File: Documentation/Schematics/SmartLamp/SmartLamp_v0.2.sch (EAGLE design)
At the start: 26 parts, among them IC1 DS3231/SO, J1 POWER_JACKPTH_BREAD, Q1 IRF1404, Q2 IRF1404, Q3 IRF1404, U1 HM-10

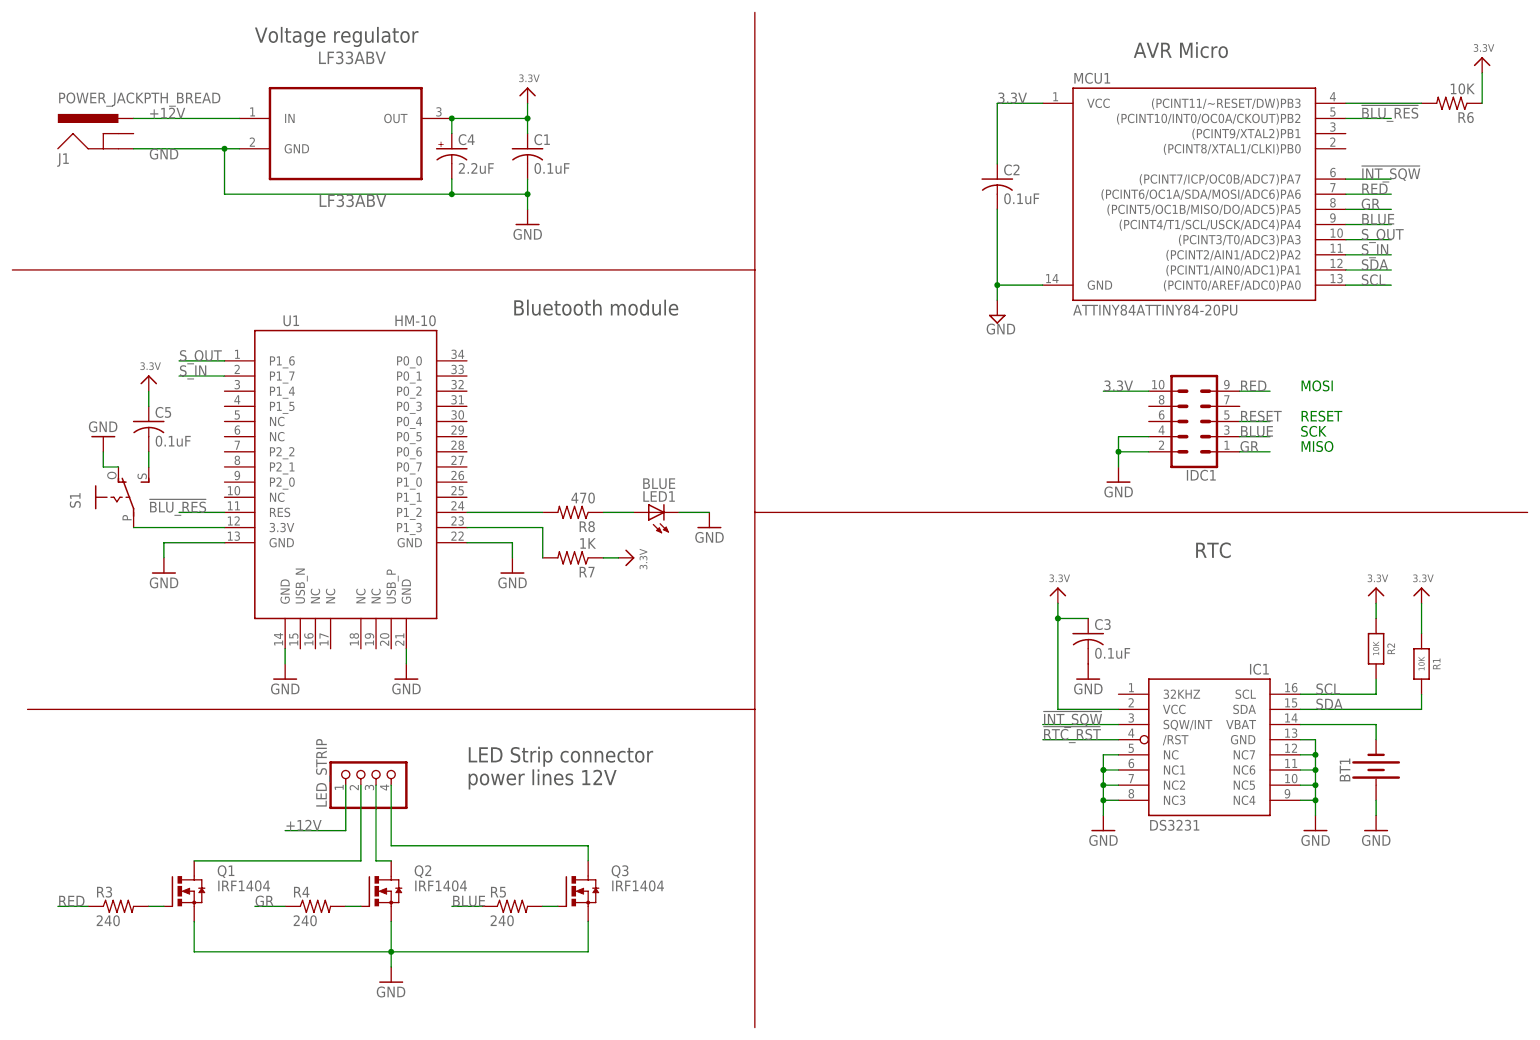
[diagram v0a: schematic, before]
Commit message: Modified switch and RGB connection
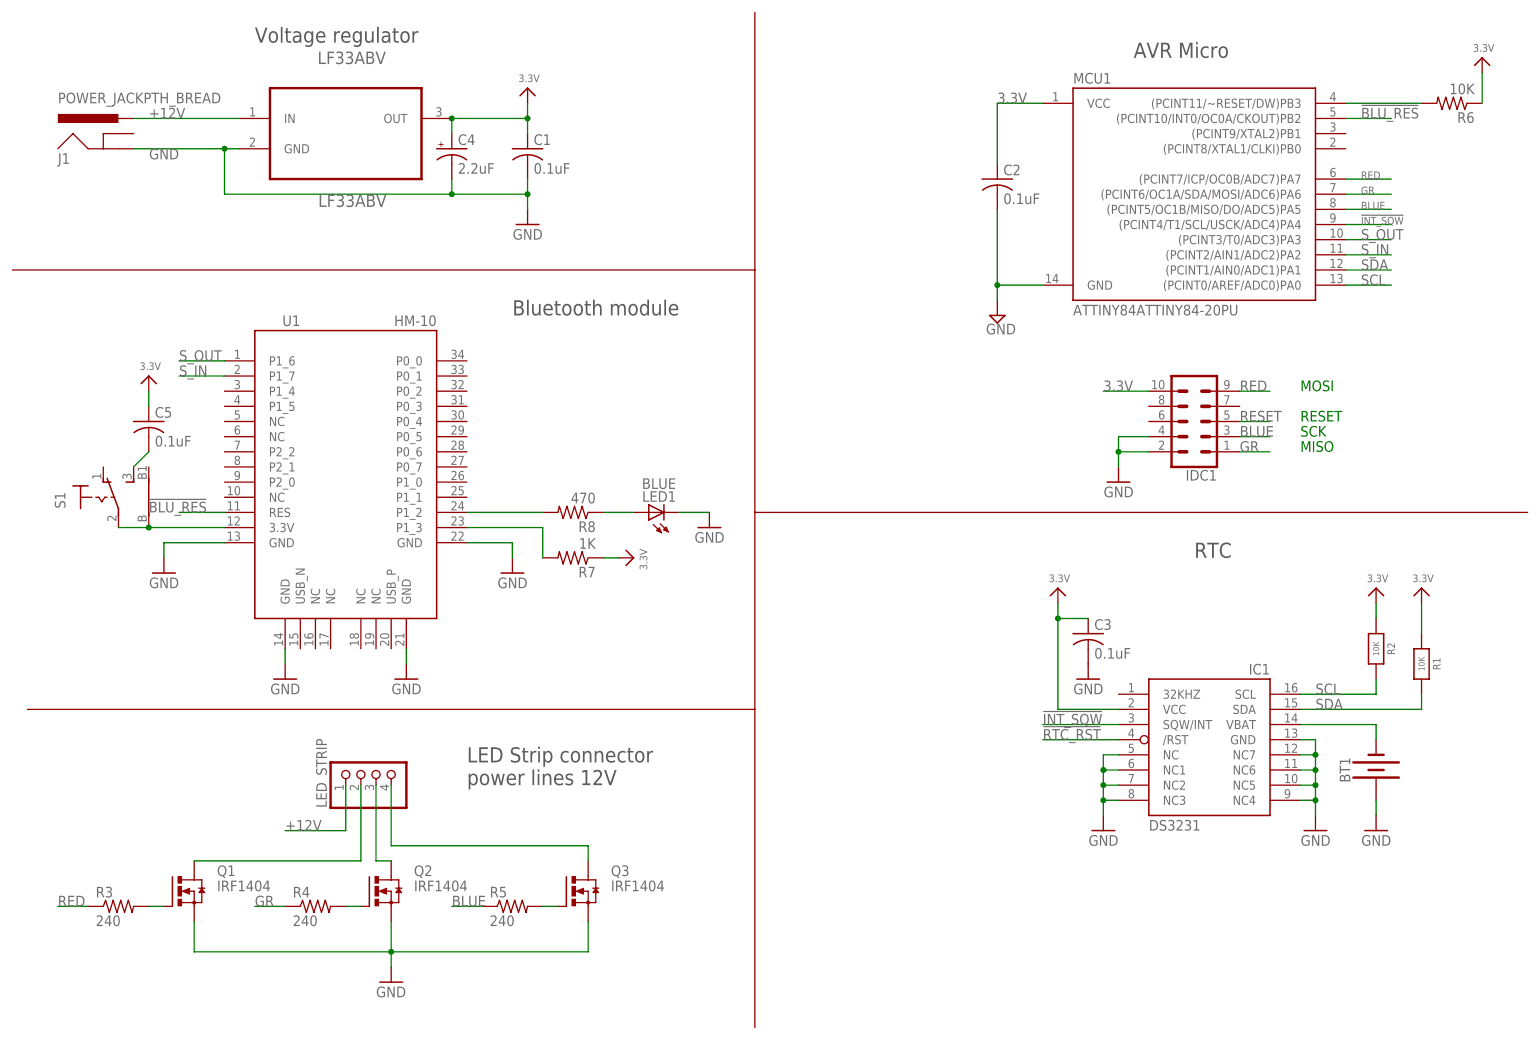
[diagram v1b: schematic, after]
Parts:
- S1: device adafruit:EG1218S -> switch:9070-1W
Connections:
- net !INT_SQW: now also MCU1.(PCINT4/T1/SCL/USCK/ADC4)PA4; no longer MCU1.(PCINT7/ICP/OC0B/ADC7)PA7
- net BLUE: now also MCU1.(PCINT5/OC1B/MISO/DO/ADC5)PA5; no longer MCU1.(PCINT4/T1/SCL/USCK/ADC4)PA4
- net GND: no longer S1.O
- net GR: now also MCU1.(PCINT6/OC1A/SDA/MOSI/ADC6)PA6; no longer MCU1.(PCINT5/OC1B/MISO/DO/ADC5)PA5
- net N$1: now also S1.B
- net RED: now also MCU1.(PCINT7/ICP/OC0B/ADC7)PA7; no longer MCU1.(PCINT6/OC1A/SDA/MOSI/ADC6)PA6
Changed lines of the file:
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@@
 <part name="U$8" library="microbuilder" deviceset="3.3V" device=""/>
 <part name="C5" library="adafruit" deviceset="C-US" device="025-024X044" value="0.1uF"/>
-<part name="S1" library="adafruit" deviceset="EG1218" device="S"/>
-<part name="GND6" library="supply1" deviceset="GND" device=""/>
+<part name="S1" library="switch" deviceset="9070-1W" device=""/>
 <part name="Q1" library="transistor-power" deviceset="IRFI540NPBF" device="" value="IRF1404"/>
 <part name="Q2" library="transistor-power" deviceset="IRFI540NPBF" device="" value="IRF1404"/>
@@
 <instance part="U$8" gate="G$1" x="106.68" y="83.82" rot="R270"/>
 <instance part="C5" gate="G$1" x="25.4" y="106.68"/>
-<instance part="S1" gate="1" x="20.32" y="93.98"/>
-<instance part="GND6" gate="1" x="17.78" y="104.14" rot="MR180"/>
+<instance part="S1" gate="2" x="17.78" y="93.98"/>
 <instance part="Q1" gate="G$1" x="30.48" y="27.94"/>
 <instance part="Q2" gate="G$1" x="63.5" y="27.94"/>
@@
 </segment>
 <segment>
-<pinref part="S1" gate="1" pin="O"/>
-<pinref part="GND6" gate="1" pin="GND"/>
-<wire x1="20.32" y1="99.06" x2="17.78" y2="99.06" width="0.1524" layer="91"/>
-<wire x1="17.78" y1="99.06" x2="17.78" y2="101.6" width="0.1524" layer="91"/>
-</segment>
-<segment>
 <pinref part="Q1" gate="G$1" pin="S"/>
 <wire x1="33.02" y1="22.86" x2="33.02" y2="17.78" width="0.1524" layer="91"/>
@@
 </segment>
 <segment>
-<pinref part="MCU1" gate="G$1" pin="(PCINT7/ICP/OC0B/ADC7)PA7"/>
-<wire x1="226.06" y1="147.32" x2="233.68" y2="147.32" width="0.1524" layer="91"/>
-<label x="228.6" y="147.32" size="1.778" layer="95"/>
+<pinref part="MCU1" gate="G$1" pin="(PCINT4/T1/SCL/USCK/ADC4)PA4"/>
+<wire x1="226.06" y1="139.7" x2="233.68" y2="139.7" width="0.1524" layer="91"/>
+<label x="228.6" y="139.7" size="1.27" layer="95" font="vector"/>
 </segment>
 </net>
@@
 <net name="N$1" class="0">
 <segment>
-<pinref part="S1" gate="1" pin="P"/>
+<pinref part="S1" gate="2" pin="P"/>
 <pinref part="U1" gate="G$1" pin="3.3V"/>
-<wire x1="22.86" y1="88.9" x2="38.1" y2="88.9" width="0.1524" layer="91"/>
+<wire x1="20.32" y1="88.9" x2="25.4" y2="88.9" width="0.1524" layer="91"/>
+<pinref part="S1" gate="2" pin="B"/>
+<wire x1="25.4" y1="88.9" x2="38.1" y2="88.9" width="0.1524" layer="91"/>
+<junction x="25.4" y="88.9"/>
 </segment>
 </net>
@@
 <segment>
 <pinref part="C5" gate="G$1" pin="2"/>
-<pinref part="S1" gate="1" pin="S"/>
-<wire x1="25.4" y1="101.6" x2="25.4" y2="99.06" width="0.1524" layer="91"/>
+<pinref part="S1" gate="2" pin="S"/>
+<wire x1="25.4" y1="101.6" x2="22.86" y2="99.06" width="0.1524" layer="91"/>
 </segment>
 </net>
@@
 </segment>
 <segment>
-<pinref part="MCU1" gate="G$1" pin="(PCINT6/OC1A/SDA/MOSI/ADC6)PA6"/>
-<wire x1="226.06" y1="144.78" x2="233.68" y2="144.78" width="0.1524" layer="91"/>
-<label x="228.6" y="144.78" size="1.778" layer="95"/>
-</segment>
-<segment>
 <pinref part="IDC1" gate="G$1" pin="9"/>
 <wire x1="208.28" y1="111.76" x2="213.36" y2="111.76" width="0.1524" layer="91"/>
 <label x="208.28" y="111.76" size="1.778" layer="95"/>
 </segment>
+<segment>
+<pinref part="MCU1" gate="G$1" pin="(PCINT7/ICP/OC0B/ADC7)PA7"/>
+<wire x1="226.06" y1="147.32" x2="233.68" y2="147.32" width="0.1524" layer="91"/>
+<label x="228.6" y="147.32" size="1.27" layer="95" font="vector"/>
+</segment>
 </net>
 <net name="GR" class="0">
@@
 </segment>
 <segment>
-<pinref part="MCU1" gate="G$1" pin="(PCINT5/OC1B/MISO/DO/ADC5)PA5"/>
-<wire x1="226.06" y1="142.24" x2="233.68" y2="142.24" width="0.1524" layer="91"/>
-<label x="228.6" y="142.24" size="1.778" layer="95"/>
-</segment>
-<segment>
 <pinref part="IDC1" gate="G$1" pin="1"/>
 <wire x1="208.28" y1="101.6" x2="213.36" y2="101.6" width="0.1524" layer="91"/>
 <label x="208.28" y="101.6" size="1.778" layer="95"/>
 </segment>
+<segment>
+<pinref part="MCU1" gate="G$1" pin="(PCINT6/OC1A/SDA/MOSI/ADC6)PA6"/>
+<wire x1="226.06" y1="144.78" x2="233.68" y2="144.78" width="0.1524" layer="91"/>
+<label x="228.6" y="144.78" size="1.27" layer="95" font="vector"/>
+</segment>
 </net>
 <net name="BLUE" class="0">
@@
 </segment>
 <segment>
-<pinref part="MCU1" gate="G$1" pin="(PCINT4/T1/SCL/USCK/ADC4)PA4"/>
-<wire x1="226.06" y1="139.7" x2="233.68" y2="139.7" width="0.1524" layer="91"/>
-<label x="228.6" y="139.7" size="1.778" layer="95"/>
-</segment>
-<segment>
 <pinref part="IDC1" gate="G$1" pin="3"/>
 <wire x1="208.28" y1="104.14" x2="213.36" y2="104.14" width="0.1524" layer="91"/>
 <label x="208.28" y="104.14" size="1.778" layer="95"/>
 </segment>
-</net>
+<segment>
+<pinref part="MCU1" gate="G$1" pin="(PCINT5/OC1B/MISO/DO/ADC5)PA5"/>
+<wire x1="226.06" y1="142.24" x2="233.68" y2="142.24" width="0.1524" layer="91"/>
+<label x="228.6" y="142.24" size="1.27" layer="95" font="vector"/>
+</segment>
+</net>

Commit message: Fixed IDC connector and replaced switch
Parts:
- removed S1: (no value), switch:9070-1W
- added S2: 219-02, switch-dil:219-02
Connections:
- new net S_OUT_DEBUG: IDC1.6, MCU1.(PCINT9/XTAL2)PB1
- net !INT_SQW: now also IDC1.7
- net 3.3V: now also IDC1.2, S2.1; no longer C5.1, IDC1.10
- net BLUE: now also IDC1.9; no longer IDC1.3
- net GND: now also IDC1.10, IDC1.8; no longer IDC1.2, IDC1.4
- net N$1: now also C5.2; no longer S1.B, S1.P
- net N$2: now also C5.1, S2.4; no longer C5.2, S1.S
- net RED: no longer IDC1.9
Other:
- moved on the sheet: C5, IDC1
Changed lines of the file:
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@@
 <part name="U$8" library="microbuilder" deviceset="3.3V" device=""/>
 <part name="C5" library="adafruit" deviceset="C-US" device="025-024X044" value="0.1uF"/>
-<part name="S1" library="switch" deviceset="9070-1W" device=""/>
 <part name="Q1" library="transistor-power" deviceset="IRFI540NPBF" device="" value="IRF1404"/>
 <part name="Q2" library="transistor-power" deviceset="IRFI540NPBF" device="" value="IRF1404"/>
@@
 <part name="BT1" library="SparkFun-Batteries" deviceset="BATTERY" device="-20MM_SMD_4LEGS"/>
 <part name="GND13" library="supply1" deviceset="GND" device=""/>
+<part name="S2" library="switch-dil" deviceset="219-02*" device=""/>
 </parts>
 <sheets>
 <sheet>
 <plain>
-<text x="218.44" y="111.76" size="1.778" layer="91">MOSI</text>
-<text x="218.44" y="104.14" size="1.778" layer="91">SCK</text>
-<text x="218.44" y="101.6" size="1.778" layer="91">MISO</text>
-<text x="218.44" y="106.68" size="1.778" layer="91">RESET</text>
+<text x="172.72" y="111.76" size="1.778" layer="91">MOSI</text>
+<text x="172.72" y="104.14" size="1.778" layer="91">SCK</text>
+<text x="172.72" y="101.6" size="1.778" layer="91">MISO</text>
+<text x="172.72" y="106.68" size="1.778" layer="91">RESET</text>
 <wire x1="2.54" y1="132.08" x2="127" y2="132.08" width="0.1524" layer="94"/>
 <wire x1="127" y1="132.08" x2="127" y2="175.26" width="0.1524" layer="94"/>
@@
 <instance part="R8" gate="G$1" x="96.52" y="91.44" rot="R180"/>
 <instance part="LED1" gate="G$1" x="109.22" y="91.44" rot="R90"/>
-<instance part="U$7" gate="G$1" x="25.4" y="114.3"/>
+<instance part="U$7" gate="G$1" x="15.24" y="121.92"/>
 <instance part="GND7" gate="1" x="27.94" y="81.28" rot="MR0"/>
 <instance part="GND8" gate="1" x="48.26" y="63.5" rot="MR0"/>
@@
 <instance part="GND12" gate="1" x="119.38" y="88.9" rot="MR0"/>
 <instance part="U$8" gate="G$1" x="106.68" y="83.82" rot="R270"/>
-<instance part="C5" gate="G$1" x="25.4" y="106.68"/>
-<instance part="S1" gate="2" x="17.78" y="93.98"/>
+<instance part="C5" gate="G$1" x="15.24" y="96.52"/>
 <instance part="Q1" gate="G$1" x="30.48" y="27.94"/>
 <instance part="Q2" gate="G$1" x="63.5" y="27.94"/>
@@
 <instance part="R4" gate="G$1" x="53.34" y="25.4"/>
 <instance part="R5" gate="G$1" x="86.36" y="25.4"/>
-<instance part="IDC1" gate="G$1" x="200.66" y="106.68" rot="R180"/>
-<instance part="GND14" gate="1" x="187.96" y="96.52" rot="MR0"/>
+<instance part="IDC1" gate="G$1" x="200.66" y="106.68"/>
+<instance part="GND14" gate="1" x="215.9" y="96.52" rot="MR0"/>
 <instance part="J1" gate="G$1" x="20.32" y="149.86"/>
 <instance part="C1" gate="G$1" x="88.9" y="152.4"/>
@@
 <instance part="BT1" gate="G$1" x="231.14" y="48.26" rot="R90"/>
 <instance part="GND13" gate="1" x="231.14" y="38.1" rot="MR0"/>
+<instance part="S2" gate="G$1" x="15.24" y="109.22" rot="R180"/>
 </instances>
 <busses>
@@
 </segment>
 <segment>
-<pinref part="IDC1" gate="G$1" pin="4"/>
-<wire x1="193.04" y1="104.14" x2="187.96" y2="104.14" width="0.1524" layer="91"/>
-<pinref part="IDC1" gate="G$1" pin="2"/>
-<wire x1="193.04" y1="101.6" x2="187.96" y2="101.6" width="0.1524" layer="91"/>
-<wire x1="187.96" y1="101.6" x2="187.96" y2="104.14" width="0.1524" layer="91"/>
-<wire x1="187.96" y1="101.6" x2="187.96" y2="99.06" width="0.1524" layer="91"/>
-<junction x="187.96" y="101.6"/>
-<pinref part="GND14" gate="1" pin="GND"/>
-</segment>
-<segment>
 <pinref part="GND4" gate="1" pin="GND"/>
 <pinref part="C3" gate="G$1" pin="2"/>
@@
 <pinref part="GND13" gate="1" pin="GND"/>
 <wire x1="231.14" y1="43.18" x2="231.14" y2="40.64" width="0.1524" layer="91"/>
+</segment>
+<segment>
+<pinref part="IDC1" gate="G$1" pin="8"/>
+<wire x1="208.28" y1="104.14" x2="215.9" y2="104.14" width="0.1524" layer="91"/>
+<pinref part="IDC1" gate="G$1" pin="10"/>
+<wire x1="208.28" y1="101.6" x2="215.9" y2="101.6" width="0.1524" layer="91"/>
+<wire x1="215.9" y1="101.6" x2="215.9" y2="104.14" width="0.1524" layer="91"/>
+<pinref part="GND14" gate="1" pin="GND"/>
+<wire x1="215.9" y1="101.6" x2="215.9" y2="99.06" width="0.1524" layer="91"/>
+<junction x="215.9" y="101.6"/>
 </segment>
 </net>
@@
 </segment>
 <segment>
+<pinref part="IDC1" gate="G$1" pin="2"/>
+<wire x1="208.28" y1="111.76" x2="215.9" y2="111.76" width="0.1524" layer="91"/>
+<label x="210.82" y="111.76" size="1.778" layer="95" font="vector"/>
+</segment>
+<segment>
 <pinref part="U$7" gate="G$1" pin="3.3V"/>
-<pinref part="C5" gate="G$1" pin="1"/>
-<wire x1="25.4" y1="111.76" x2="25.4" y2="109.22" width="0.1524" layer="91"/>
-</segment>
-<segment>
-<pinref part="IDC1" gate="G$1" pin="10"/>
-<wire x1="193.04" y1="111.76" x2="185.42" y2="111.76" width="0.1524" layer="91"/>
-<label x="185.42" y="111.76" size="1.778" layer="95"/>
+<pinref part="S2" gate="G$1" pin="1"/>
+<wire x1="15.24" y1="119.38" x2="15.24" y2="116.84" width="0.1524" layer="91"/>
 </segment>
 </net>
@@
 <pinref part="MCU1" gate="G$1" pin="(PCINT4/T1/SCL/USCK/ADC4)PA4"/>
 <wire x1="226.06" y1="139.7" x2="233.68" y2="139.7" width="0.1524" layer="91"/>
-<label x="228.6" y="139.7" size="1.27" layer="95" font="vector"/>
+<label x="228.6" y="139.7" size="1.778" layer="95" font="vector"/>
+</segment>
+<segment>
+<pinref part="IDC1" gate="G$1" pin="7"/>
+<wire x1="193.04" y1="104.14" x2="182.88" y2="104.14" width="0.1524" layer="91"/>
+<label x="182.88" y="104.14" size="1.778" layer="95" font="vector"/>
 </segment>
 </net>
@@
 <pinref part="R6" gate="G$1" pin="2"/>
 <wire x1="226.06" y1="160.02" x2="238.76" y2="160.02" width="0.1524" layer="91"/>
+<label x="228.6" y="160.02" size="1.778" layer="95"/>
 </segment>
 <segment>
 <pinref part="IDC1" gate="G$1" pin="5"/>
-<wire x1="208.28" y1="106.68" x2="213.36" y2="106.68" width="0.1524" layer="91"/>
-<label x="208.28" y="106.68" size="1.778" layer="95"/>
+<wire x1="193.04" y1="106.68" x2="182.88" y2="106.68" width="0.1524" layer="91"/>
+<label x="182.88" y="106.68" size="1.778" layer="95" font="vector"/>
 </segment>
 </net>
@@
 <pinref part="R7" gate="G$1" pin="2"/>
 <wire x1="91.44" y1="88.9" x2="91.44" y2="83.82" width="0.1524" layer="91"/>
-</segment>
-</net>
-<net name="N$1" class="0">
-<segment>
-<pinref part="S1" gate="2" pin="P"/>
-<pinref part="U1" gate="G$1" pin="3.3V"/>
-<wire x1="20.32" y1="88.9" x2="25.4" y2="88.9" width="0.1524" layer="91"/>
-<pinref part="S1" gate="2" pin="B"/>
-<wire x1="25.4" y1="88.9" x2="38.1" y2="88.9" width="0.1524" layer="91"/>
-<junction x="25.4" y="88.9"/>
-</segment>
-</net>
-<net name="N$2" class="0">
-<segment>
-<pinref part="C5" gate="G$1" pin="2"/>
-<pinref part="S1" gate="2" pin="S"/>
-<wire x1="25.4" y1="101.6" x2="22.86" y2="99.06" width="0.1524" layer="91"/>
 </segment>
 </net>
@@
 </segment>
 <segment>
-<pinref part="IDC1" gate="G$1" pin="9"/>
-<wire x1="208.28" y1="111.76" x2="213.36" y2="111.76" width="0.1524" layer="91"/>
-<label x="208.28" y="111.76" size="1.778" layer="95"/>
-</segment>
-<segment>
 <pinref part="MCU1" gate="G$1" pin="(PCINT7/ICP/OC0B/ADC7)PA7"/>
 <wire x1="226.06" y1="147.32" x2="233.68" y2="147.32" width="0.1524" layer="91"/>
-<label x="228.6" y="147.32" size="1.27" layer="95" font="vector"/>
+<label x="228.6" y="147.32" size="1.778" layer="95"/>
 </segment>
 </net>
@@
 </segment>
 <segment>
-<pinref part="IDC1" gate="G$1" pin="1"/>
-<wire x1="208.28" y1="101.6" x2="213.36" y2="101.6" width="0.1524" layer="91"/>
-<label x="208.28" y="101.6" size="1.778" layer="95"/>
-</segment>
-<segment>
 <pinref part="MCU1" gate="G$1" pin="(PCINT6/OC1A/SDA/MOSI/ADC6)PA6"/>
 <wire x1="226.06" y1="144.78" x2="233.68" y2="144.78" width="0.1524" layer="91"/>
-<label x="228.6" y="144.78" size="1.27" layer="95" font="vector"/>
+<label x="228.6" y="144.78" size="1.778" layer="95"/>
+</segment>
+<segment>
+<pinref part="IDC1" gate="G$1" pin="1"/>
+<wire x1="193.04" y1="111.76" x2="182.88" y2="111.76" width="0.1524" layer="91"/>
+<label x="182.88" y="111.76" size="1.778" layer="95" font="vector"/>
 </segment>
 </net>
@@
 </segment>
 <segment>
-<pinref part="IDC1" gate="G$1" pin="3"/>
-<wire x1="208.28" y1="104.14" x2="213.36" y2="104.14" width="0.1524" layer="91"/>
-<label x="208.28" y="104.14" size="1.778" layer="95"/>
-</segment>
-<segment>
 <pinref part="MCU1" gate="G$1" pin="(PCINT5/OC1B/MISO/DO/ADC5)PA5"/>
 <wire x1="226.06" y1="142.24" x2="233.68" y2="142.24" width="0.1524" layer="91"/>
-<label x="228.6" y="142.24" size="1.27" layer="95" font="vector"/>
+<label x="228.6" y="142.24" size="1.778" layer="95"/>
+</segment>
+<segment>
+<pinref part="IDC1" gate="G$1" pin="9"/>
+<wire x1="193.04" y1="101.6" x2="182.88" y2="101.6" width="0.1524" layer="91"/>
+<label x="182.88" y="101.6" size="1.778" layer="95" font="vector"/>
 </segment>
 </net>
@@
 </segment>
 </net>
+<net name="S_OUT_DEBUG" class="0">
+<segment>
+<pinref part="MCU1" gate="G$1" pin="(PCINT9/XTAL2)PB1"/>
+<wire x1="226.06" y1="154.94" x2="233.68" y2="154.94" width="0.1524" layer="91"/>
+<label x="228.6" y="154.94" size="1.778" layer="95" font="vector"/>
+</segment>
+<segment>
+<pinref part="IDC1" gate="G$1" pin="6"/>
+<wire x1="208.28" y1="106.68" x2="215.9" y2="106.68" width="0.1524" layer="91"/>
+<label x="210.82" y="106.68" size="1.778" layer="95" font="vector"/>
+</segment>
+</net>
+<net name="N$1" class="0">
+<segment>
+<pinref part="U1" gate="G$1" pin="3.3V"/>
+<wire x1="38.1" y1="88.9" x2="15.24" y2="88.9" width="0.1524" layer="91"/>
+<pinref part="C5" gate="G$1" pin="2"/>
+<wire x1="15.24" y1="91.44" x2="15.24" y2="88.9" width="0.1524" layer="91"/>
+</segment>
+</net>
+<net name="N$2" class="0">
+<segment>
+<pinref part="S2" gate="G$1" pin="4"/>
+<pinref part="C5" gate="G$1" pin="1"/>
+<wire x1="15.24" y1="101.6" x2="15.24" y2="99.06" width="0.1524" layer="91"/>
+</segment>
+</net>

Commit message: Revisited board, ERC on schematic
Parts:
- BT1: value (none) -> BT1
- IDC1: value (none) -> IDC1
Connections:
- removed net !RTC_RST: IC1./RST
- removed net 3.3V: C1.1, C2.1, C3.1, C4.+, IC1.VCC, IDC1.2, LF33ABV.OUT, MCU1.VCC, R1.1, R2.1, R6.1, R7.1, S2.1
- removed net N$5: BT1.-, IC1.VBAT
- new net +3V3: C1.1, C3.1, C4.+, IC1.VCC, LF33ABV.OUT, R1.1, R2.1, R6.1, R7.1, S2.1
- new net 3V3: C2.1, IDC1.2, MCU1.VCC
- new net VBAT: BT1.+, IC1.VBAT
- net GND: now also BT1.-; no longer BT1.+
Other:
- moved on the sheet: BT1
